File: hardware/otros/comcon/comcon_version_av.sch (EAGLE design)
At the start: 112 parts, among them IC10 74HC365N, IC11 74HC365N, IC12 74HC365N, IC13 74HC365N, IC14 74HC365N, IC3 74HCT32, IC7 74HC365N, IC8 74HC365N, IC9 74HC365N

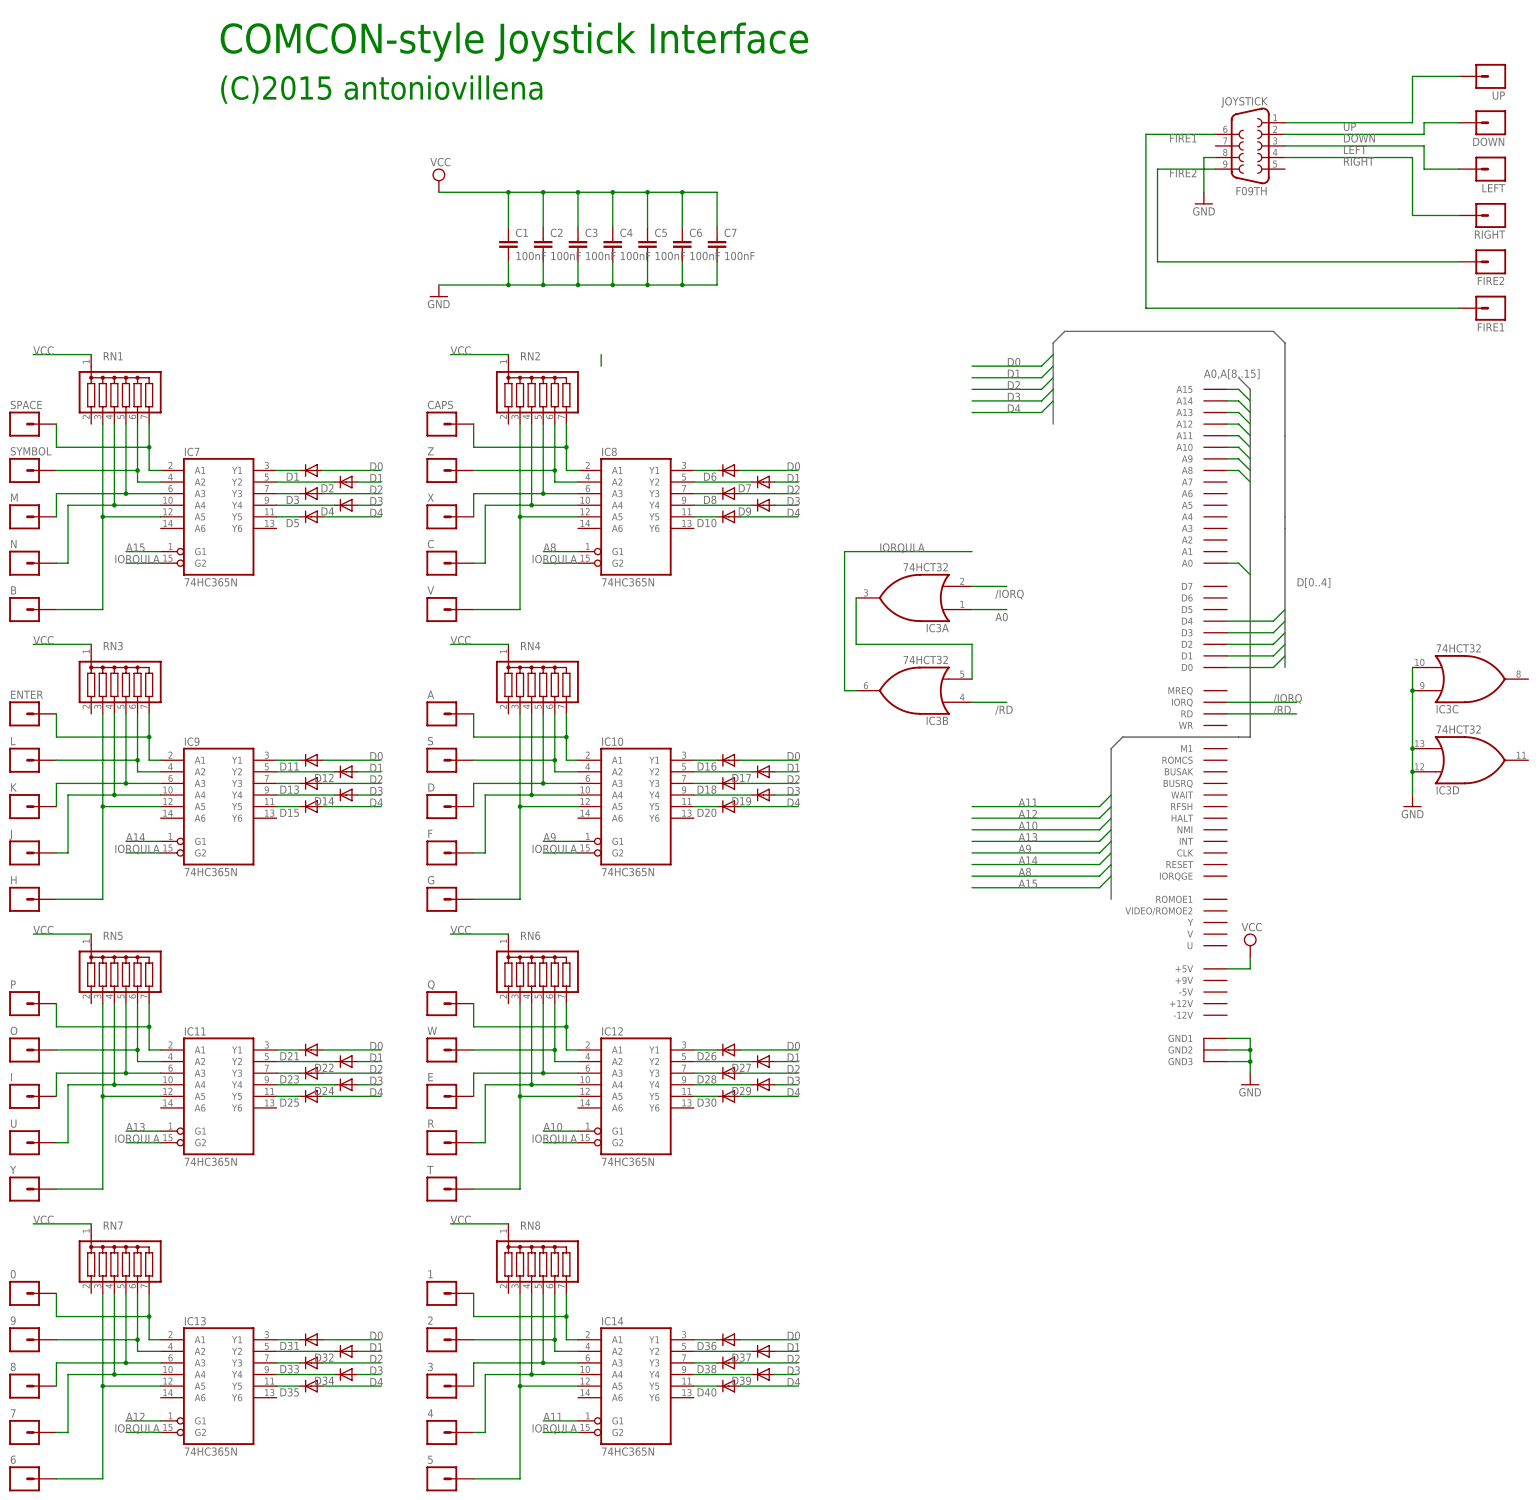
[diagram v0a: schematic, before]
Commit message: 
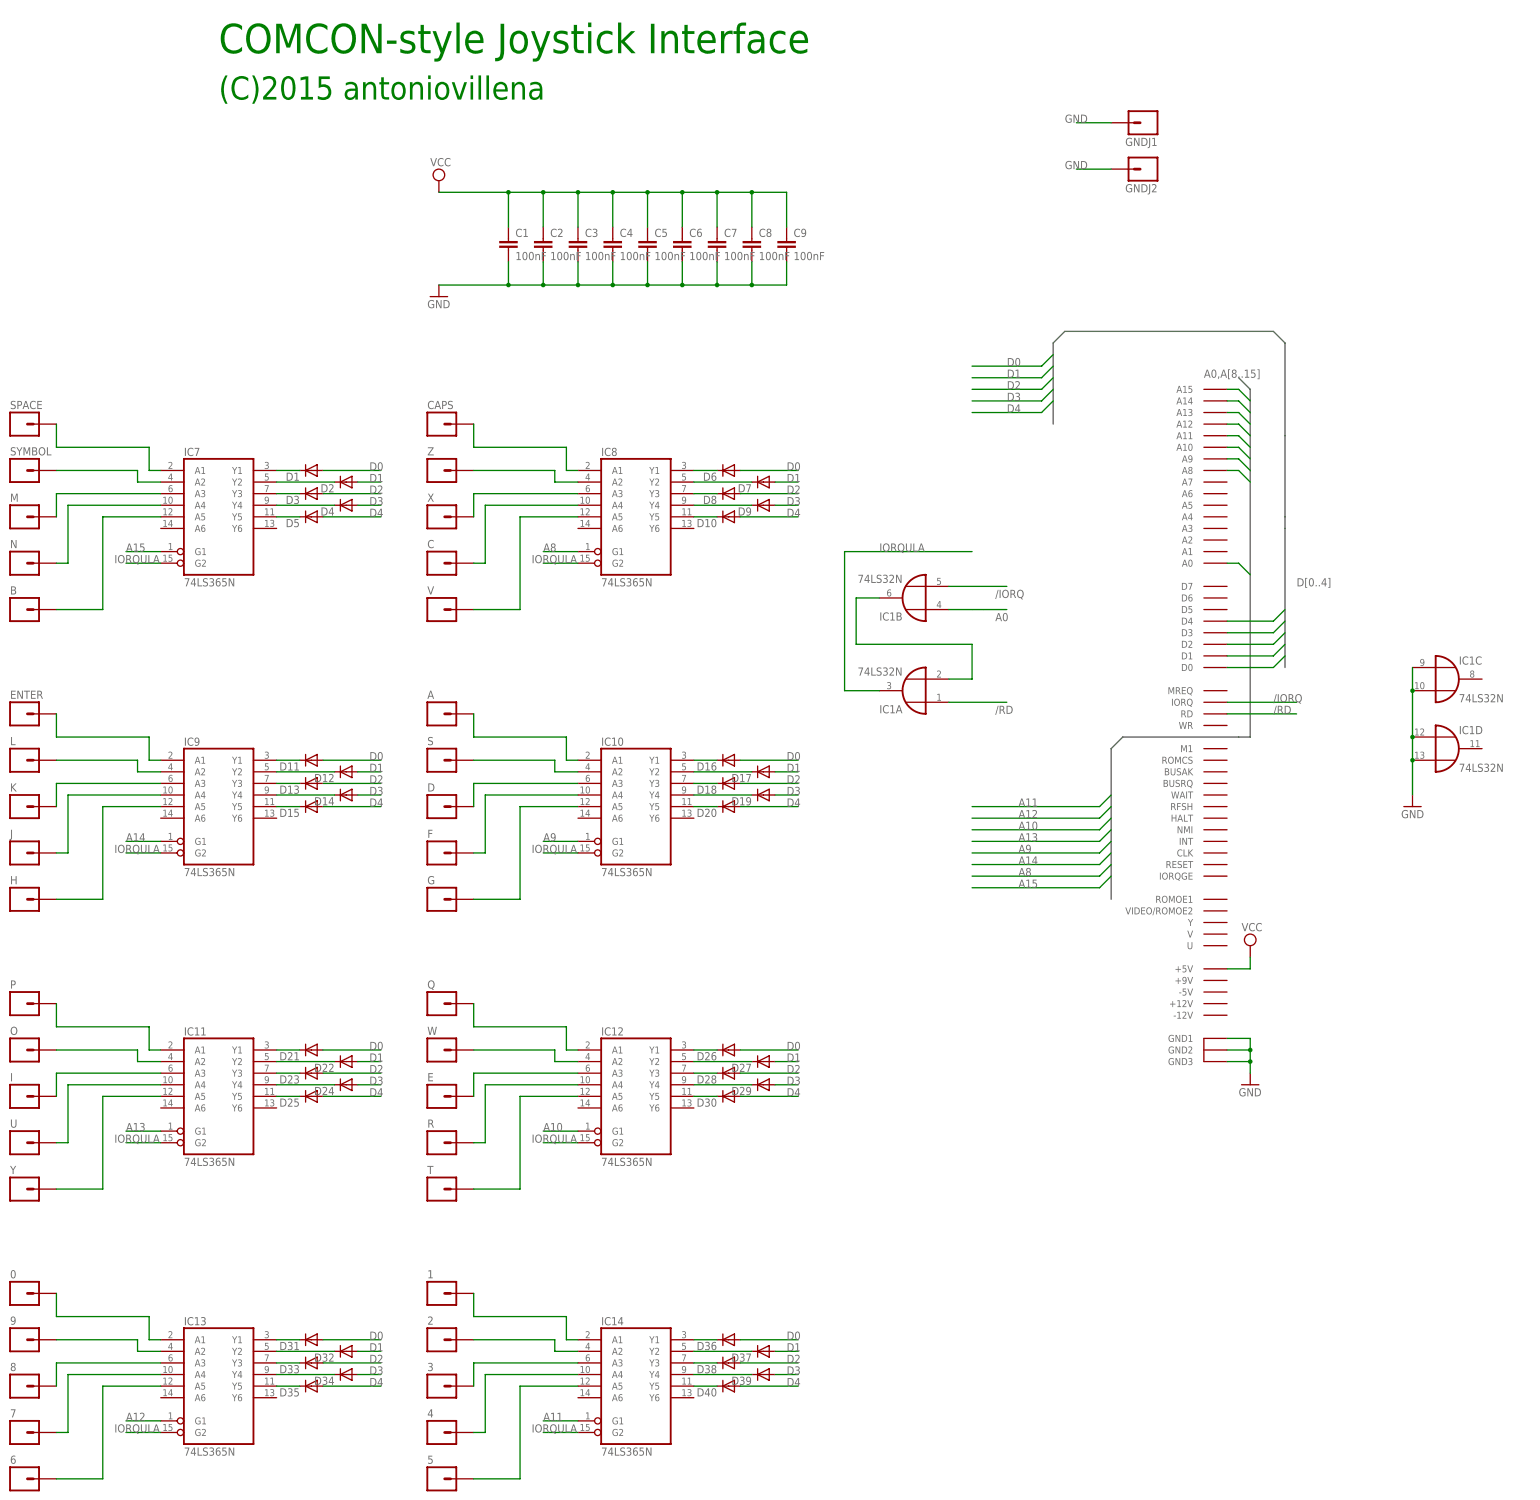
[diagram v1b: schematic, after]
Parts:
- removed DOWN, FIRE1, FIRE2, LEFT, RIGHT, UP: M01PTH, SparkFun-Connectors:M01PTH
- removed IC3: 74HCT32, 74xx-us:74LS32N
- removed JOYSTICK: F09TH, con-subd-new:F09TH
- removed RN1, RN2, RN3, RN4, RN5, RN6, RN7, RN8: (no value), resistor-sil:G06R
- added C8, C9: 100nF, rcl:C-EU050-025X075
- added GNDJ1, GNDJ2: M01PTH, SparkFun-Connectors:M01PTH
- added IC1: 74LS32N, 74xx-eu:74LS32N
- IC10, IC11, IC12, IC13, IC14, IC7, IC8, IC9: value 74HC365N -> 74LS365N
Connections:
- removed net DOWN: DOWN.1, JOYSTICK.2
- removed net FIRE1: FIRE1.1, JOYSTICK.6
- removed net FIRE2: FIRE2.1, JOYSTICK.9
- removed net LEFT: JOYSTICK.3, LEFT.1
- removed net RIGHT: JOYSTICK.4, RIGHT.1
- removed net UP: JOYSTICK.1, UP.1
- net /IORQ: now also IC1B.I1; no longer IC3A.I1
- net /RD: now also IC1A.I0; no longer IC3B.I0
- net A0: now also IC1B.I0; no longer IC3A.I0
- net GND: now also C8.2, C9.2, GNDJ1.1, GNDJ2.1, IC1C.I0, IC1C.I1, IC1D.I0, IC1D.I1; no longer IC3C.I0, IC3C.I1, IC3D.I0, IC3D.I1, JOYSTICK.8
- net IORQULA: now also IC1A.O; no longer IC3B.O
- net N$1: now also IC1A.I1, IC1B.O; no longer IC3A.O, IC3B.I1
- net N$104: no longer RN8.7
- net N$105: no longer RN8.6
- net N$106: no longer RN8.5
- net N$107: no longer RN8.4
- net N$108: no longer RN8.3
- net N$12: no longer RN1.6
- net N$18: no longer RN1.5
- net N$2: no longer RN1.7
- net N$20: no longer RN1.4
- net N$22: no longer RN1.3
- net N$25: no longer RN2.7
- net N$26: no longer RN2.6
- net N$27: no longer RN2.5
- net N$28: no longer RN2.4
- net N$47: no longer RN2.3
- net N$53: no longer RN3.7
- net N$54: no longer RN3.6
- net N$55: no longer RN3.5
- net N$56: no longer RN3.4
- net N$57: no longer RN3.3
- net N$63: no longer RN4.7
- net N$64: no longer RN4.6
- net N$65: no longer RN4.5
- net N$66: no longer RN4.4
- net N$67: no longer RN4.3
- net N$74: no longer RN5.7
- net N$75: no longer RN5.6
- net N$76: no longer RN5.5
- net N$77: no longer RN5.4
- net N$78: no longer RN5.3
- net N$84: no longer RN6.7
- net N$85: no longer RN6.6
- net N$86: no longer RN6.5
- net N$87: no longer RN6.4
- net N$88: no longer RN6.3
- net N$94: no longer RN7.7
- net N$95: no longer RN7.6
- net N$96: no longer RN7.5
- net N$97: no longer RN7.4
- net N$98: no longer RN7.3
- net VCC: now also C8.1, C9.1; no longer RN1.1, RN2.1, RN3.1, RN4.1, RN5.1, RN6.1, RN7.1, RN8.1

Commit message: 
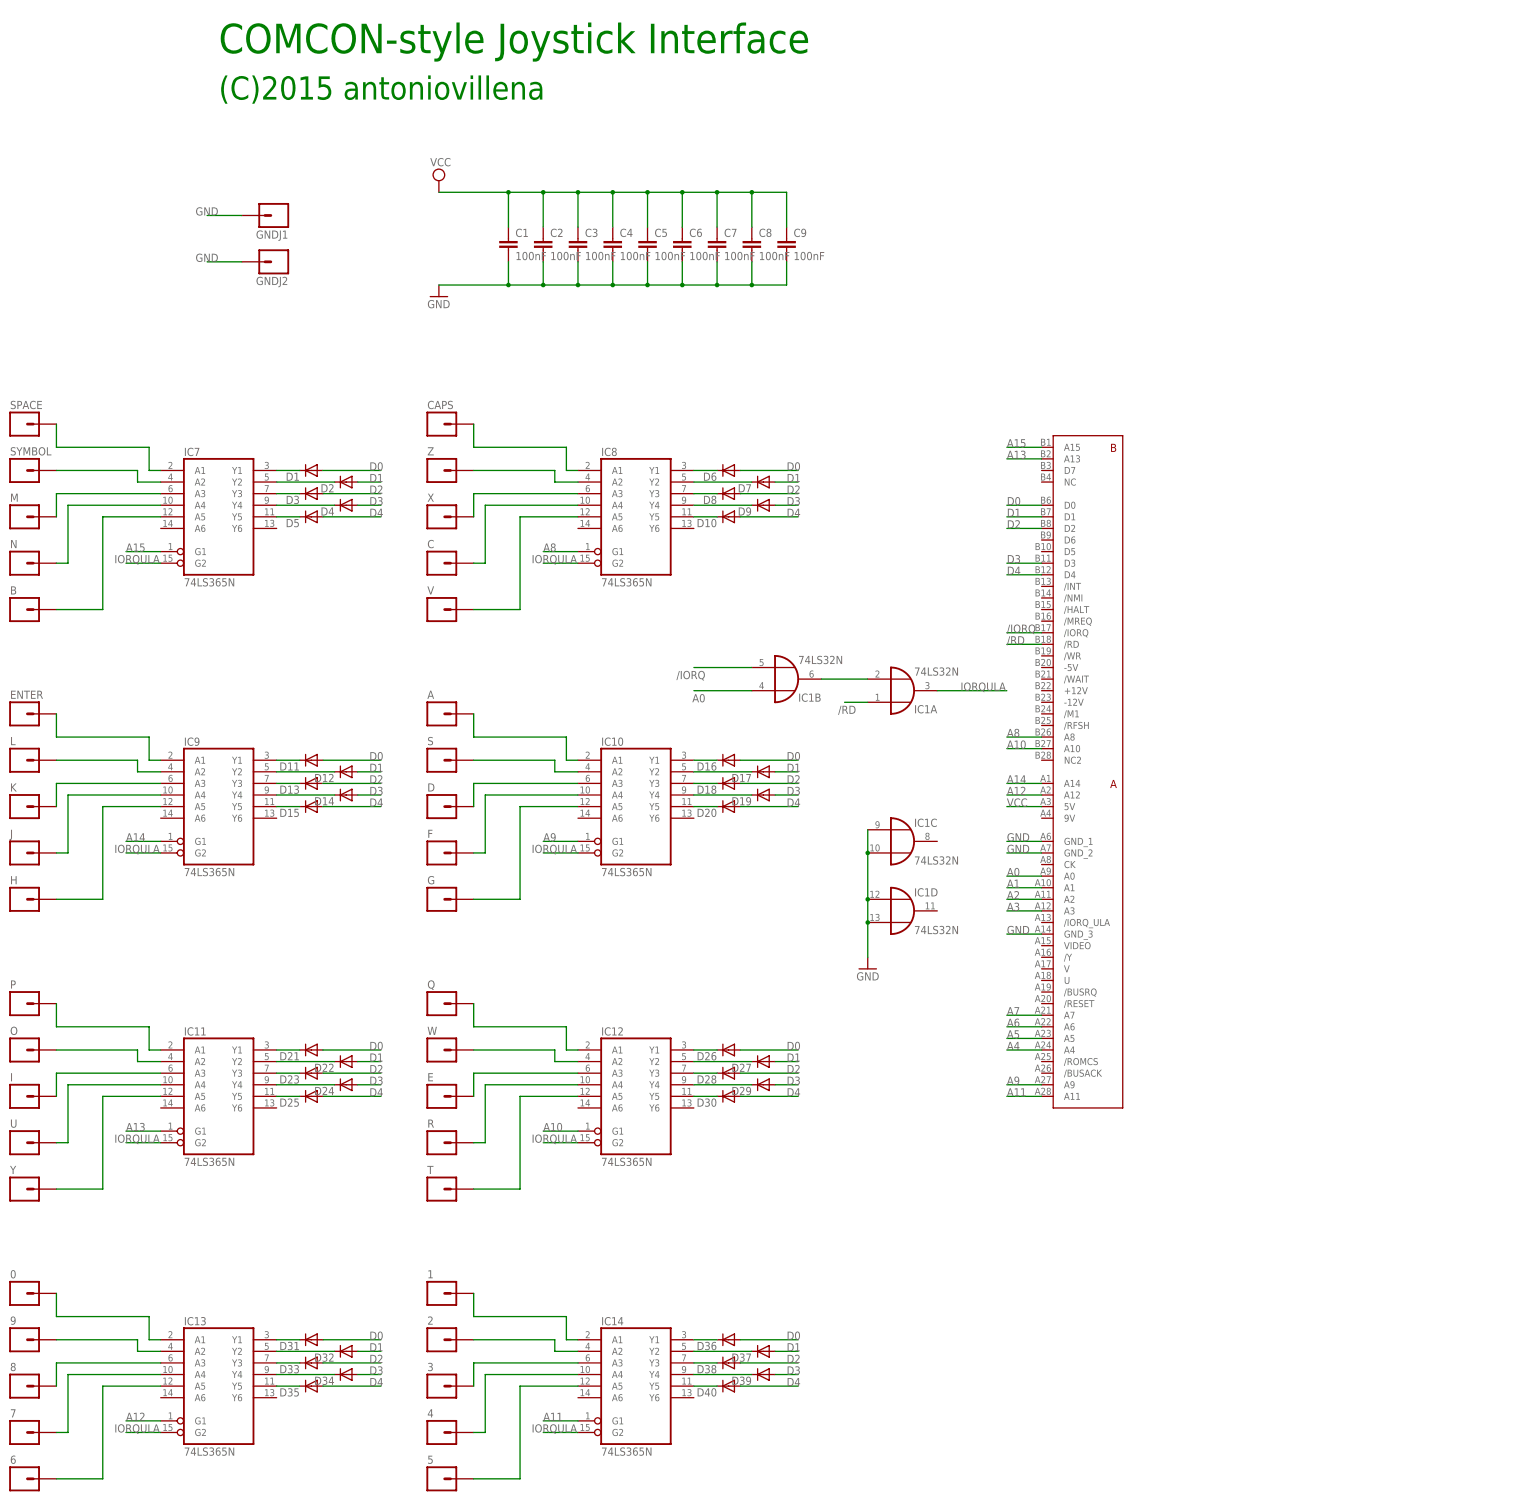
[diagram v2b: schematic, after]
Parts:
- removed ZX_BUS: CONECTOR_SPECTRUM, zx_spectrum:CONECTOR_SPECTRUM
- added U$3: (no value), zx_edge:ZXSP_ED2X28_SPE
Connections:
- new net A1: U$3.A1
- new net A2: U$3.A2
- new net A3: U$3.A3
- new net A4: U$3.A4
- new net A5: U$3.A5
- new net A6: U$3.A6
- new net A7: U$3.A7
- net /IORQ: now also U$3./IORQ; no longer ZX_BUS.IORQ
- net /RD: now also U$3./RD; no longer ZX_BUS.RD
- net A0: now also U$3.A0; no longer ZX_BUS.A0
- net A10: now also U$3.A10; no longer ZX_BUS.A10
- net A11: now also U$3.A11; no longer ZX_BUS.A11
- net A12: now also U$3.A12; no longer ZX_BUS.A12
- net A13: now also U$3.A13; no longer ZX_BUS.A13
- net A14: now also U$3.A14; no longer ZX_BUS.A14
- net A15: now also U$3.A15; no longer ZX_BUS.A15
- net A8: now also U$3.A8; no longer ZX_BUS.A8
- net A9: now also U$3.A9; no longer ZX_BUS.A9
- net D0: now also U$3.D0; no longer ZX_BUS.D0
- net D1: now also U$3.D1; no longer ZX_BUS.D1
- net D2: now also U$3.D2; no longer ZX_BUS.D2
- net D3: now also U$3.D3; no longer ZX_BUS.D3
- net D4: now also U$3.D4; no longer ZX_BUS.D4
- net GND: now also U$3.GND_1, U$3.GND_2, U$3.GND_3; no longer ZX_BUS.GND1, ZX_BUS.GND2, ZX_BUS.GND3
- net VCC: now also U$3.5V; no longer ZX_BUS.+5V
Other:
- moved on the sheet: GNDJ1, GNDJ2, IC1A, IC1B, IC1C, IC1D
